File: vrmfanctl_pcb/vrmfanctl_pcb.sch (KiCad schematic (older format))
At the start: 11 parts, among them J1 SATA Power Male, J3 Pin header L-type male, J4 Pin header L-type female, Q1 ?, U1 ATtiny85-20PU

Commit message: Use OC1A instead of OC1B. OC1B PWM output of ATTiny85 has a problem the same as ATTiny45 Rev B-C.
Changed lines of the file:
@@
 Wire Wire Line
 	1400 2300 1400 2600
-NoConn ~ 3700 1750
 Wire Wire Line
 	3100 1300 3100 1350
@@
 	1400 1200 1400 1800
 Connection ~ 1400 1800
-Text Label 3750 2050 0    50   ~ 0
-PWM#
 $Comp
 L Device:Q_NPN_ECB Q1
@@
 To Fan (KDB0305HA3-CD7)
 Wire Wire Line
-	3700 2050 3900 2050
-Wire Wire Line
-	3900 2050 3900 2400
-Wire Wire Line
 	1400 2600 1500 2600
 Wire Wire Line
@@
 Wire Wire Line
 	1500 2600 1600 2600
-Wire Wire Line
-	3700 1950 4750 1950
 Text Label 4400 2050 0    50   ~ 0
 PWM_5V
@@
 	4750 2400 4750 2250
 Connection ~ 4500 2400
+Text Label 3750 1750 0    50   ~ 0
+PWM#
+Wire Wire Line
+	3700 1950 4750 1950
+Wire Wire Line
+	3700 1750 3900 1750
+Wire Wire Line
+	3900 1750 3900 2400
+NoConn ~ 3700 2050
 $EndSCHEMATC

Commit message: supply 3.3V with M.2 SSD
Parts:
- removed D1, D2, D3: D, Diode_THT:D_T-1_P5.08mm_Horizontal, symbol Device:D
- removed Q1: ?, Package_TO_SOT_SMD:SC-59, symbol Device:Q_NPN_ECB
- removed R1: 2M, Resistor_THT:R_Axial_DIN0204_L3.6mm_D1.6mm_P5.08mm_Horizontal, symbol Device:R
- removed R2: 47K, Resistor_THT:R_Axial_DIN0204_L3.6mm_D1.6mm_P5.08mm_Horizontal, symbol Device:R
- added J2: Pin header L-shape male, Connector_PinHeader_2.54mm:PinHeader_1x01_P2.54mm_Horizontal, symbol Connector_Generic:Conn_01x01
- J3: value Pin header L-type male -> Pin header L-shape male
- J4: value Pin header L-type female -> Pin header L-shape female
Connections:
- net labels added: 3V3, PWM
- net labels removed: PWM#, PWM_5V
- wire segments 43 -> 40
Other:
- note removed: "SOT? hFE=287 CBE Vf=688mV"
- note removed: "around 3V"
- moved on the sheet: C1, J4, U1

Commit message: Add a UART header. remove an I2C interface. Add a temperature sensor.
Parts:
- removed J2: Pin header L-shape male, Connector_PinHeader_2.54mm:PinHeader_1x01_P2.54mm_Horizontal, symbol Connector_Generic:Conn_01x01
- removed J3: Pin header L-shape male, Connector_PinHeader_2.54mm:PinHeader_1x02_P2.54mm_Horizontal, symbol Connector_Generic:Conn_01x02
- removed J4: Pin header L-shape female, Connector_PinSocket_2.54mm:PinSocket_1x04_P2.54mm_Horizontal, symbol Connector_Generic:Conn_01x04
- added J2: Pin header L-shape, Connector_PinHeader_2.54mm:PinHeader_1x03_P2.54mm_Horizontal, symbol Connector:Conn_01x03_Male
- added J3: Pin socket L-shape, Connector_PinSocket_2.54mm:PinSocket_1x02_P2.54mm_Horizontal, symbol Connector:Conn_01x02_Female
- added J4: Pin socket L-shape, Connector_PinSocket_2.54mm:PinSocket_1x04_P2.54mm_Horizontal, symbol Connector:Conn_01x04_Female
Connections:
- net labels added: RX, TEMP, TX
- net labels removed: 3V3, SCL, SDA
- wire segments 40 -> 46
- no-connect marks 11 -> 10
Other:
- note added: "5V±5%"
- note added: "To temperature sensor diode"
- note removed: "To SMBus DDR4 SO-DIMM Pin 254(SDA), Pin 253(SCL)"
- moved on the sheet: C1, J1, U1

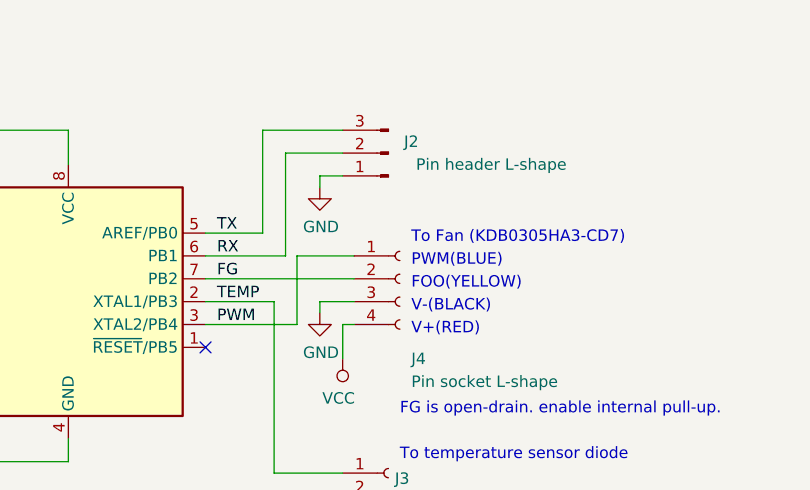
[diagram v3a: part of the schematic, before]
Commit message: Use through hole instead of pin header
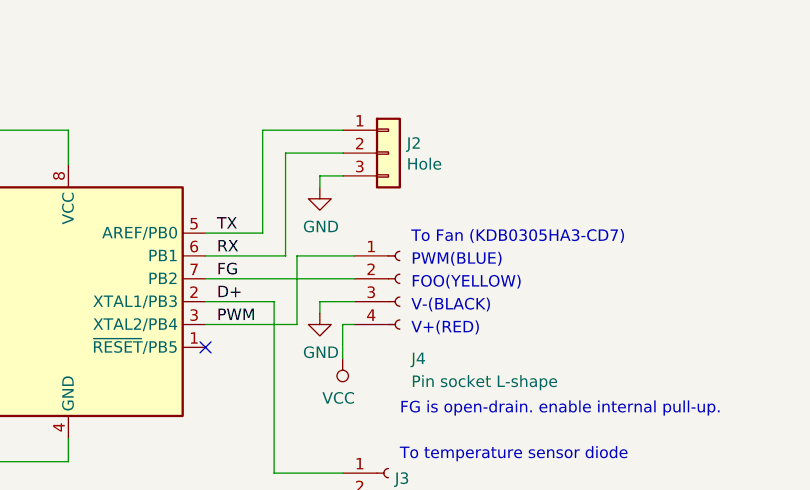
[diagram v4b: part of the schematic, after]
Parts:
- removed J2: Pin header L-shape, Connector_PinHeader_2.54mm:PinHeader_1x03_P2.54mm_Horizontal, symbol Connector:Conn_01x03_Male
- added J2: Hole, Connector_PinHeader_2.54mm:PinHeader_1x03_P2.54mm_Vertical, symbol Connector_Generic:Conn_01x03
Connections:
- net GND: now also J2.3 (Pin_3)
- net RX: now also J2.2 (Pin_2)
- net TX: now also J2.1 (Pin_1)
- net TEMP renamed D+
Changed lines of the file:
@@
 EESchema Schematic File Version 4
 LIBS:vrmfanctl_pcb-cache
-EELAYER 30 0
+EELAYER 26 0
 EELAYER END
 $Descr A4 11693 8268
@@
 $EndComp
 $Comp
-L Connector:Conn_01x03_Male J2
-U 1 1 5D5FAC0C
-P 5900 1450
-F 0 "J2" H 5800 1400 50  0000 C CNN
-F 1 "Pin header L-shape" H 5450 1500 50  0000 C CNN
-F 2 "Connector_PinHeader_2.54mm:PinHeader_1x03_P2.54mm_Horizontal" H 5900 1450 50  0001 C CNN
-F 3 "~" H 5900 1450 50  0001 C CNN
-	1    5900 1450
-	-1   0    0    1
-$EndComp
-$Comp
 L power:GND #PWR06
 U 1 1 5D600CEB
@@
 To temperature sensor diode
 Text Label 5150 2100 0    50   ~ 0
-TEMP
+D+
 Wire Wire Line
 	5400 2850 5700 2850
@@
 Wire Wire Line
 	5400 2100 5400 2850
+$Comp
+L Connector_Generic:Conn_01x03 J2
+U 1 1 5D5D4A8F
+P 5900 1450
+F 0 "J2" H 5980 1492 50  0000 L CNN
+F 1 "Hole" H 5980 1401 50  0000 L CNN
+F 2 "Connector_PinHeader_2.54mm:PinHeader_1x03_P2.54mm_Vertical" H 5900 1450 50  0001 C CNN
+F 3 "~" H 5900 1450 50  0001 C CNN
+	1    5900 1450
+	1    0    0    -1
+$EndComp
 $EndSCHEMATC

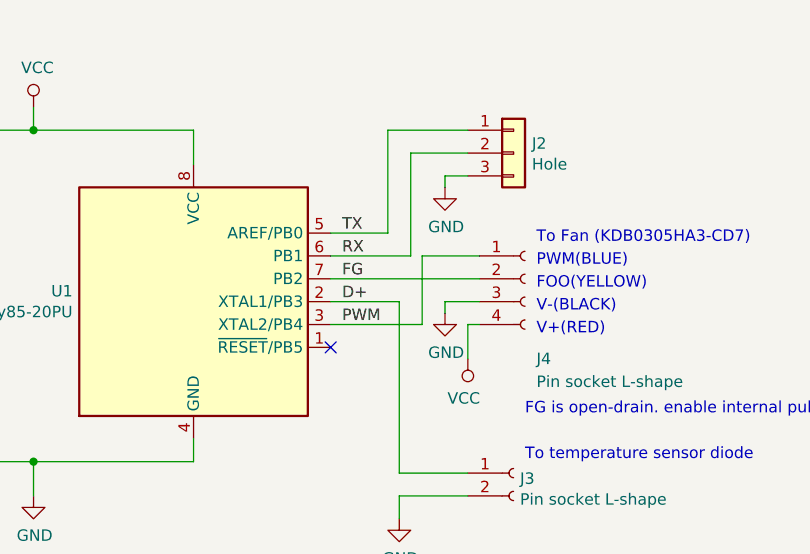
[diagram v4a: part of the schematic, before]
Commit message: remove unneeded FG wire
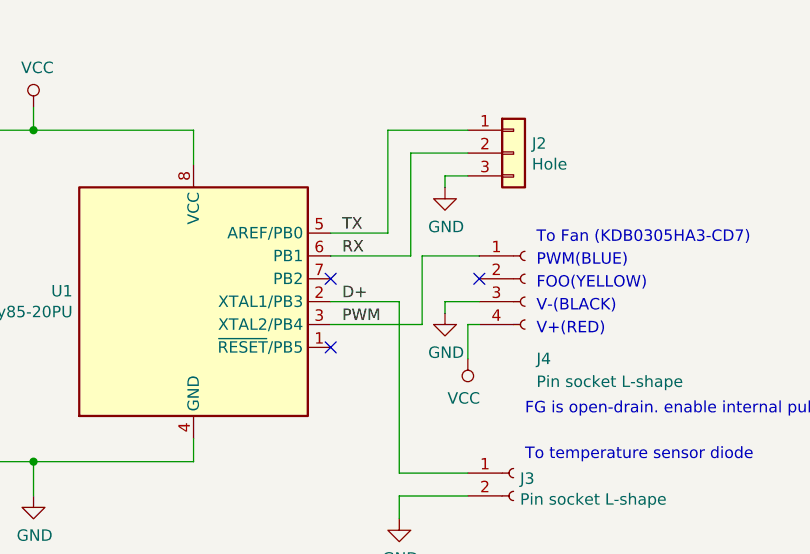
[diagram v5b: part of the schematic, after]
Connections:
- net FG: no longer names the net of U1.7 (PB2)
- net FG: no longer J4.2 (Pin_2)
- no-connect marks 10 -> 12
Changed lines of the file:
@@
 Wire Wire Line
 	1650 3350 1650 3300
-Text Label 5150 2000 0    50   ~ 0
-FG
 NoConn ~ 5100 2300
 $Comp
@@
 	-1   0    0    1
 $EndComp
-Wire Wire Line
-	5100 2000 5750 2000
 $Comp
 L Connector:Conn_01x04_Female J4
@@
 	1    0    0    -1
 $EndComp
+NoConn ~ 5100 2000
+NoConn ~ 5750 2000
 $EndSCHEMATC

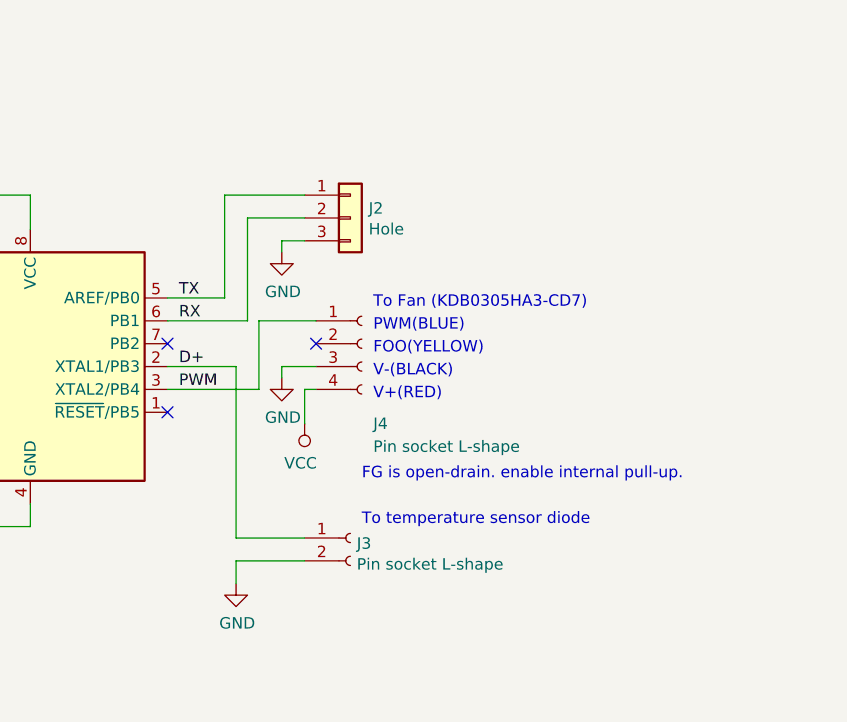
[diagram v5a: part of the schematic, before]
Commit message: add reset pin to the header
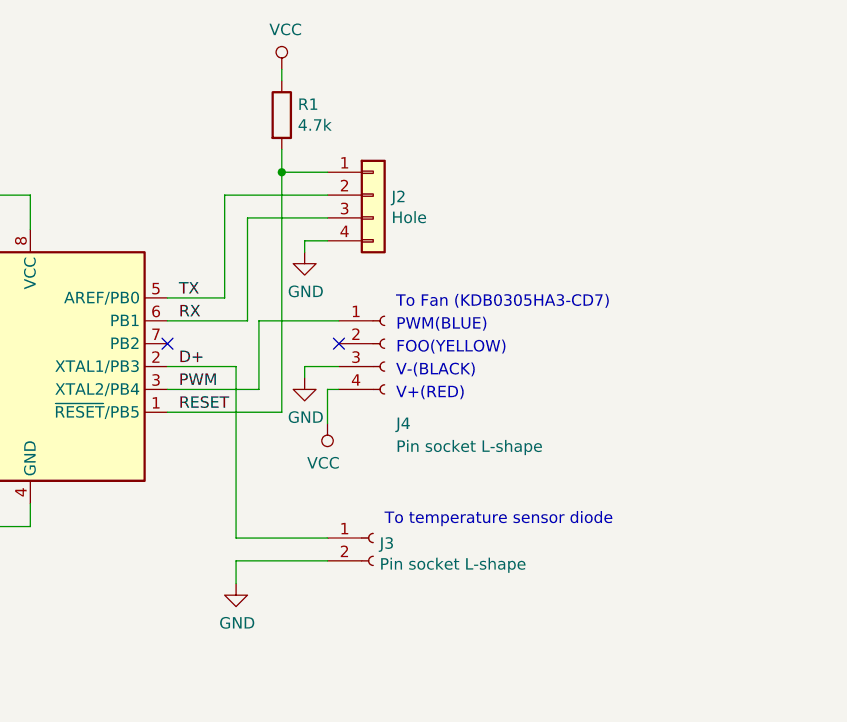
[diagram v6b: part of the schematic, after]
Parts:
- removed J2: Hole, Connector_PinHeader_2.54mm:PinHeader_1x03_P2.54mm_Vertical, symbol Connector_Generic:Conn_01x03
- added J2: Hole, Connector_PinHeader_2.54mm:PinHeader_1x04_P2.54mm_Vertical, symbol Connector_Generic:Conn_01x04
- added R1: 4.7k, Resistor_THT:R_Axial_DIN0204_L3.6mm_D1.6mm_P5.08mm_Horizontal, symbol Device:R
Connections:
- net GND: now also J2.4 (Pin_4)
- net RX: now also J2.3 (Pin_3)
- net TX: now also J2.2 (Pin_2)
- net VCC: now also R1.1
- net RESET: now reaches U1.1 (~RESET~/PB5)
- net RESET: now also J2.1 (Pin_1), R1.2
- no-connect marks 12 -> 11
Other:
- note removed: "FG is open-drain. enable internal pull-up."
- moved on the sheet: J3, J4
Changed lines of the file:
@@
 Wire Wire Line
 	1650 3350 1650 3300
-NoConn ~ 5100 2300
 $Comp
 L power:GND #PWR0101
@@
 	1    0    0    -1
 $EndComp
-Text Notes 6000 1950 0    50   ~ 0
+Text Notes 6100 1950 0    50   ~ 0
 PWM(BLUE)
-Text Notes 6000 2050 0    50   ~ 0
+Text Notes 6100 2050 0    50   ~ 0
 FOO(YELLOW)
-Text Notes 6000 2150 0    50   ~ 0
+Text Notes 6100 2150 0    50   ~ 0
 V-(BLACK)
-Text Notes 6000 2250 0    50   ~ 0
+Text Notes 6100 2250 0    50   ~ 0
 V+(RED)
-Text Notes 6000 1850 0    50   ~ 0
+Text Notes 6100 1850 0    50   ~ 0
 To Fan (KDB0305HA3-CD7)
-Text Notes 5950 2600 0    50   ~ 0
-FG is open-drain. enable internal pull-up.
 Text Label 5150 2200 0    50   ~ 0
 PWM
 Wire Wire Line
-	5600 2100 5750 2100
-Wire Wire Line
-	5600 2100 5600 2150
+	5700 2100 5850 2100
+Wire Wire Line
+	5700 2100 5700 2150
 Wire Wire Line
 	4500 1350 4500 1500
 Wire Wire Line
-	5700 2200 5750 2200
+	5800 2200 5850 2200
 Text Notes 1100 2050 0    50   ~ 0
 5V±5%
@@
 $EndComp
 Wire Wire Line
-	5700 2200 5700 2350
+	5800 2200 5800 2350
 Wire Wire Line
 	3800 1250 3800 1350
@@
 L power:GND #PWR07
 U 1 1 5D5E75C4
-P 5600 2150
-F 0 "#PWR07" H 5600 1900 50  0001 C CNN
-F 1 "GND" H 5605 1977 50  0000 C CNN
-F 2 "" H 5600 2150 50  0001 C CNN
-F 3 "" H 5600 2150 50  0001 C CNN
-	1    5600 2150
+P 5700 2150
+F 0 "#PWR07" H 5700 1900 50  0001 C CNN
+F 1 "GND" H 5705 1977 50  0000 C CNN
+F 2 "" H 5700 2150 50  0001 C CNN
+F 3 "" H 5700 2150 50  0001 C CNN
+	1    5700 2150
 	1    0    0    -1
 $EndComp
@@
 L power:VCC #PWR08
 U 1 1 5D5EAA48
-P 5700 2350
-F 0 "#PWR08" H 5700 2200 50  0001 C CNN
-F 1 "VCC" H 5718 2523 50  0000 C CNN
-F 2 "" H 5700 2350 50  0001 C CNN
-F 3 "" H 5700 2350 50  0001 C CNN
-	1    5700 2350
+P 5800 2350
+F 0 "#PWR08" H 5800 2200 50  0001 C CNN
+F 1 "VCC" H 5818 2523 50  0000 C CNN
+F 2 "" H 5800 2350 50  0001 C CNN
+F 3 "" H 5800 2350 50  0001 C CNN
+	1    5800 2350
 	-1   0    0    1
 $EndComp
@@
 L Connector:Conn_01x04_Female J4
 U 1 1 5D5F6860
-P 5950 2000
-F 0 "J4" H 6000 1650 50  0000 L CNN
-F 1 "Pin socket L-shape" H 6000 1550 50  0000 L CNN
-F 2 "Connector_PinSocket_2.54mm:PinSocket_1x04_P2.54mm_Horizontal" H 5950 2000 50  0001 C CNN
-F 3 "~" H 5950 2000 50  0001 C CNN
-	1    5950 2000
+P 6050 2000
+F 0 "J4" H 6100 1650 50  0000 L CNN
+F 1 "Pin socket L-shape" H 6100 1550 50  0000 L CNN
+F 2 "Connector_PinSocket_2.54mm:PinSocket_1x04_P2.54mm_Horizontal" H 6050 2000 50  0001 C CNN
+F 3 "~" H 6050 2000 50  0001 C CNN
+	1    6050 2000
 	1    0    0    -1
 $EndComp
@@
 L power:GND #PWR06
 U 1 1 5D600CEB
-P 5600 1600
-F 0 "#PWR06" H 5600 1350 50  0001 C CNN
-F 1 "GND" H 5605 1427 50  0000 C CNN
-F 2 "" H 5600 1600 50  0001 C CNN
-F 3 "" H 5600 1600 50  0001 C CNN
-	1    5600 1600
-	1    0    0    -1
-$EndComp
-Wire Wire Line
-	5700 1550 5600 1550
-Wire Wire Line
-	5600 1550 5600 1600
+P 5700 1600
+F 0 "#PWR06" H 5700 1350 50  0001 C CNN
+F 1 "GND" H 5705 1427 50  0000 C CNN
+F 2 "" H 5700 1600 50  0001 C CNN
+F 3 "" H 5700 1600 50  0001 C CNN
+	1    5700 1600
+	1    0    0    -1
+$EndComp
+Wire Wire Line
+	5800 1550 5700 1550
+Wire Wire Line
+	5700 1550 5700 1600
 Wire Wire Line
 	5350 1350 5350 1800
@@
 	5350 1800 5100 1800
 Wire Wire Line
-	5350 1350 5700 1350
+	5350 1350 5800 1350
 Text Label 5150 1800 0    50   ~ 0
 TX
@@
 	5450 1900 5450 1450
 Wire Wire Line
-	5450 1450 5700 1450
-Wire Wire Line
-	5750 1900 5500 1900
-Text Notes 5950 2800 0    50   ~ 0
+	5450 1450 5800 1450
+Wire Wire Line
+	5850 1900 5500 1900
+Text Notes 6050 2800 0    50   ~ 0
 To temperature sensor diode
 Text Label 5150 2100 0    50   ~ 0
 D+
 Wire Wire Line
-	5400 2850 5700 2850
+	5400 2850 5800 2850
 Wire Wire Line
 	5400 2950 5400 3050
 Wire Wire Line
-	5700 2950 5400 2950
+	5800 2950 5400 2950
 $Comp
 L power:GND #PWR05
@@
 L Connector:Conn_01x02_Female J3
 U 1 1 5D610DF4
-P 5900 2850
-F 0 "J3" H 5928 2826 50  0000 L CNN
-F 1 "Pin socket L-shape" H 5928 2735 50  0000 L CNN
-F 2 "Connector_PinSocket_2.54mm:PinSocket_1x02_P2.54mm_Horizontal" H 5900 2850 50  0001 C CNN
-F 3 "~" H 5900 2850 50  0001 C CNN
-	1    5900 2850
+P 6000 2850
+F 0 "J3" H 6028 2826 50  0000 L CNN
+F 1 "Pin socket L-shape" H 6028 2735 50  0000 L CNN
+F 2 "Connector_PinSocket_2.54mm:PinSocket_1x02_P2.54mm_Horizontal" H 6000 2850 50  0001 C CNN
+F 3 "~" H 6000 2850 50  0001 C CNN
+	1    6000 2850
 	1    0    0    -1
 $EndComp
@@
 	5500 2200 5400 2200
 Wire Wire Line
+	5400 2200 5100 2200
+Wire Wire Line
+	5400 2100 5100 2100
+Wire Wire Line
+	5400 2100 5400 2850
+NoConn ~ 5100 2000
+NoConn ~ 5850 2000
+$Comp
+L Device:R R1
+U 1 1 5D62348B
+P 5600 1000
+F 0 "R1" H 5670 1046 50  0000 L CNN
+F 1 "4.7k" H 5670 955 50  0000 L CNN
+F 2 "Resistor_THT:R_Axial_DIN0204_L3.6mm_D1.6mm_P5.08mm_Horizontal" V 5530 1000 50  0001 C CNN
+F 3 "~" H 5600 1000 50  0001 C CNN
+	1    5600 1000
+	1    0    0    -1
+$EndComp
+$Comp
+L Connector_Generic:Conn_01x04 J2
+U 1 1 5D6235F9
+P 6000 1350
+F 0 "J2" H 6080 1342 50  0000 L CNN
+F 1 "Hole" H 6080 1251 50  0000 L CNN
+F 2 "Connector_PinHeader_2.54mm:PinHeader_1x04_P2.54mm_Vertical" H 6000 1350 50  0001 C CNN
+F 3 "~" H 6000 1350 50  0001 C CNN
+	1    6000 1350
+	1    0    0    -1
+$EndComp
+$Comp
+L power:VCC #PWR0103
+U 1 1 5D623D93
+P 5600 800
+F 0 "#PWR0103" H 5600 650 50  0001 C CNN
+F 1 "VCC" H 5617 973 50  0000 C CNN
+F 2 "" H 5600 800 50  0001 C CNN
+F 3 "" H 5600 800 50  0001 C CNN
+	1    5600 800
+	1    0    0    -1
+$EndComp
+Wire Wire Line
+	5600 800  5600 850
+Wire Wire Line
+	5600 1150 5600 1250
+Wire Wire Line
+	5600 1250 5800 1250
+Wire Wire Line
 	5500 1900 5500 2200
 Wire Wire Line
-	5400 2200 5100 2200
-Wire Wire Line
-	5400 2100 5100 2100
-Wire Wire Line
-	5400 2100 5400 2850
-$Comp
-L Connector_Generic:Conn_01x03 J2
-U 1 1 5D5D4A8F
-P 5900 1450
-F 0 "J2" H 5980 1492 50  0000 L CNN
-F 1 "Hole" H 5980 1401 50  0000 L CNN
-F 2 "Connector_PinHeader_2.54mm:PinHeader_1x03_P2.54mm_Vertical" H 5900 1450 50  0001 C CNN
-F 3 "~" H 5900 1450 50  0001 C CNN
-	1    5900 1450
-	1    0    0    -1
-$EndComp
-NoConn ~ 5100 2000
-NoConn ~ 5750 2000
+	5600 1250 5600 2300
+Wire Wire Line
+	5600 2300 5100 2300
+Connection ~ 5600 1250
+Text Label 5150 2300 0    50   ~ 0
+RESET
 $EndSCHEMATC
